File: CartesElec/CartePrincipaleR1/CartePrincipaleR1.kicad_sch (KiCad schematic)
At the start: 21 parts, among them J1 I2C, J11 Conn_01x02_Male, J12 Conn_01x04_Male, J13 Conn_01x04_Male, J2 I2C, J3 UART, J4 UART, J5 Conn_02x08_Top_Bottom, J6 Conn_02x08_Top_Bottom, J8 Conn_01x04_Male, U1 LT1129-3.3_SOT223, U2 NUCLEO64-F411RE

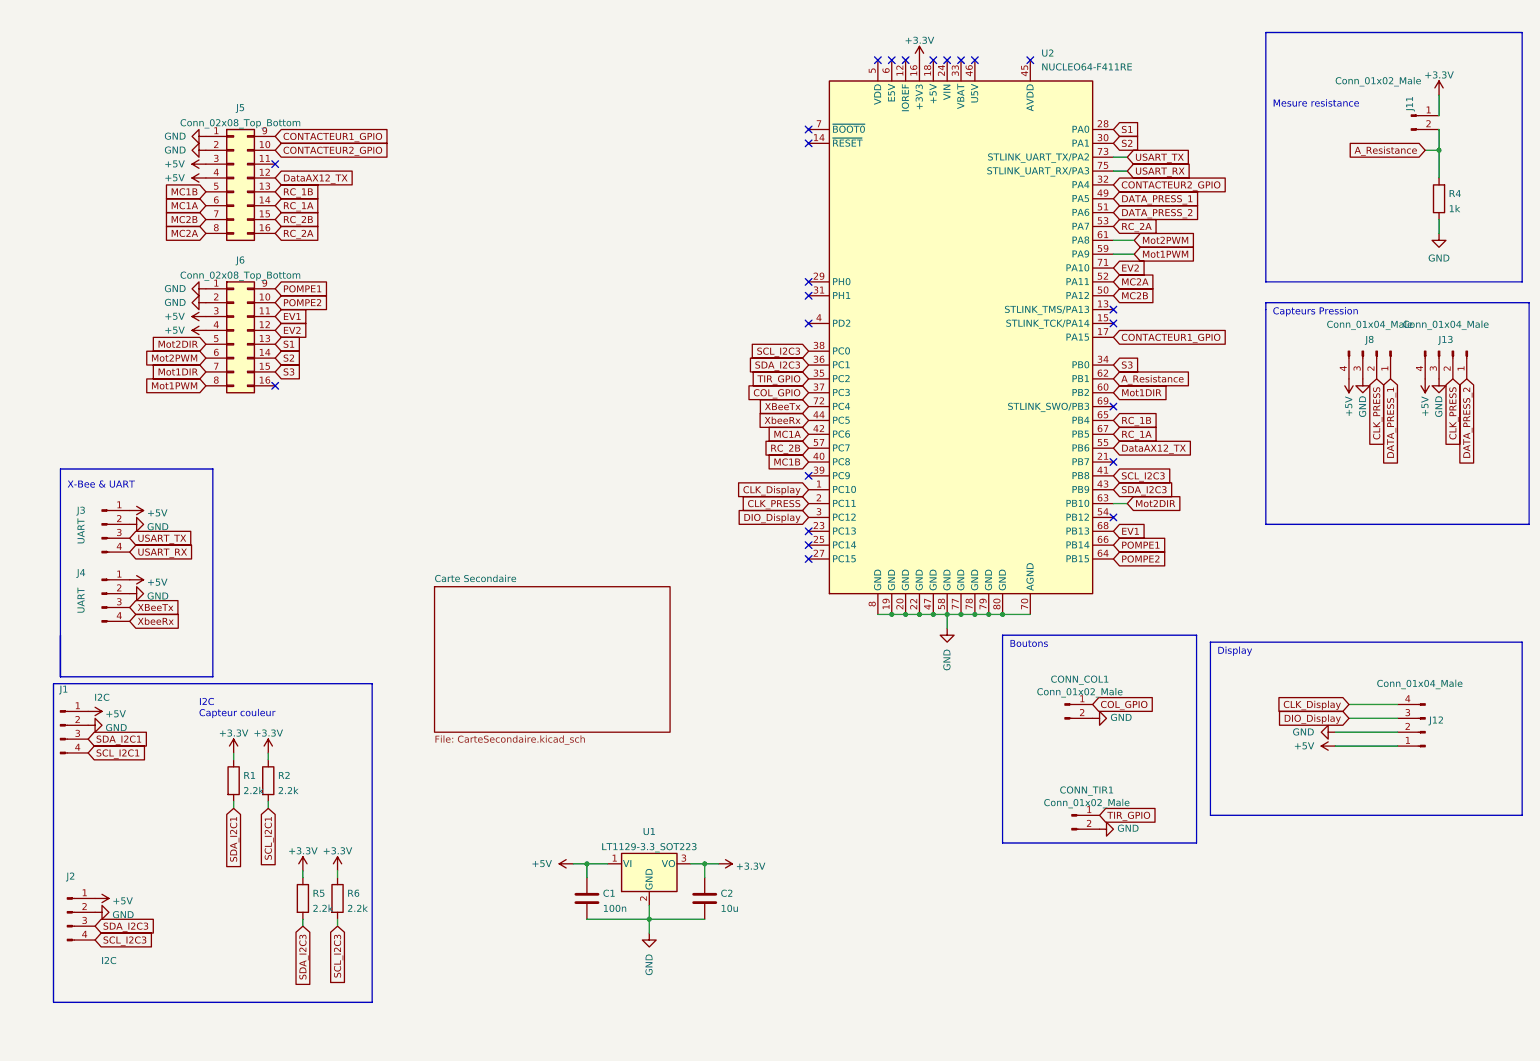
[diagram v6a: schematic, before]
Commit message: Ajout de textes au PCB
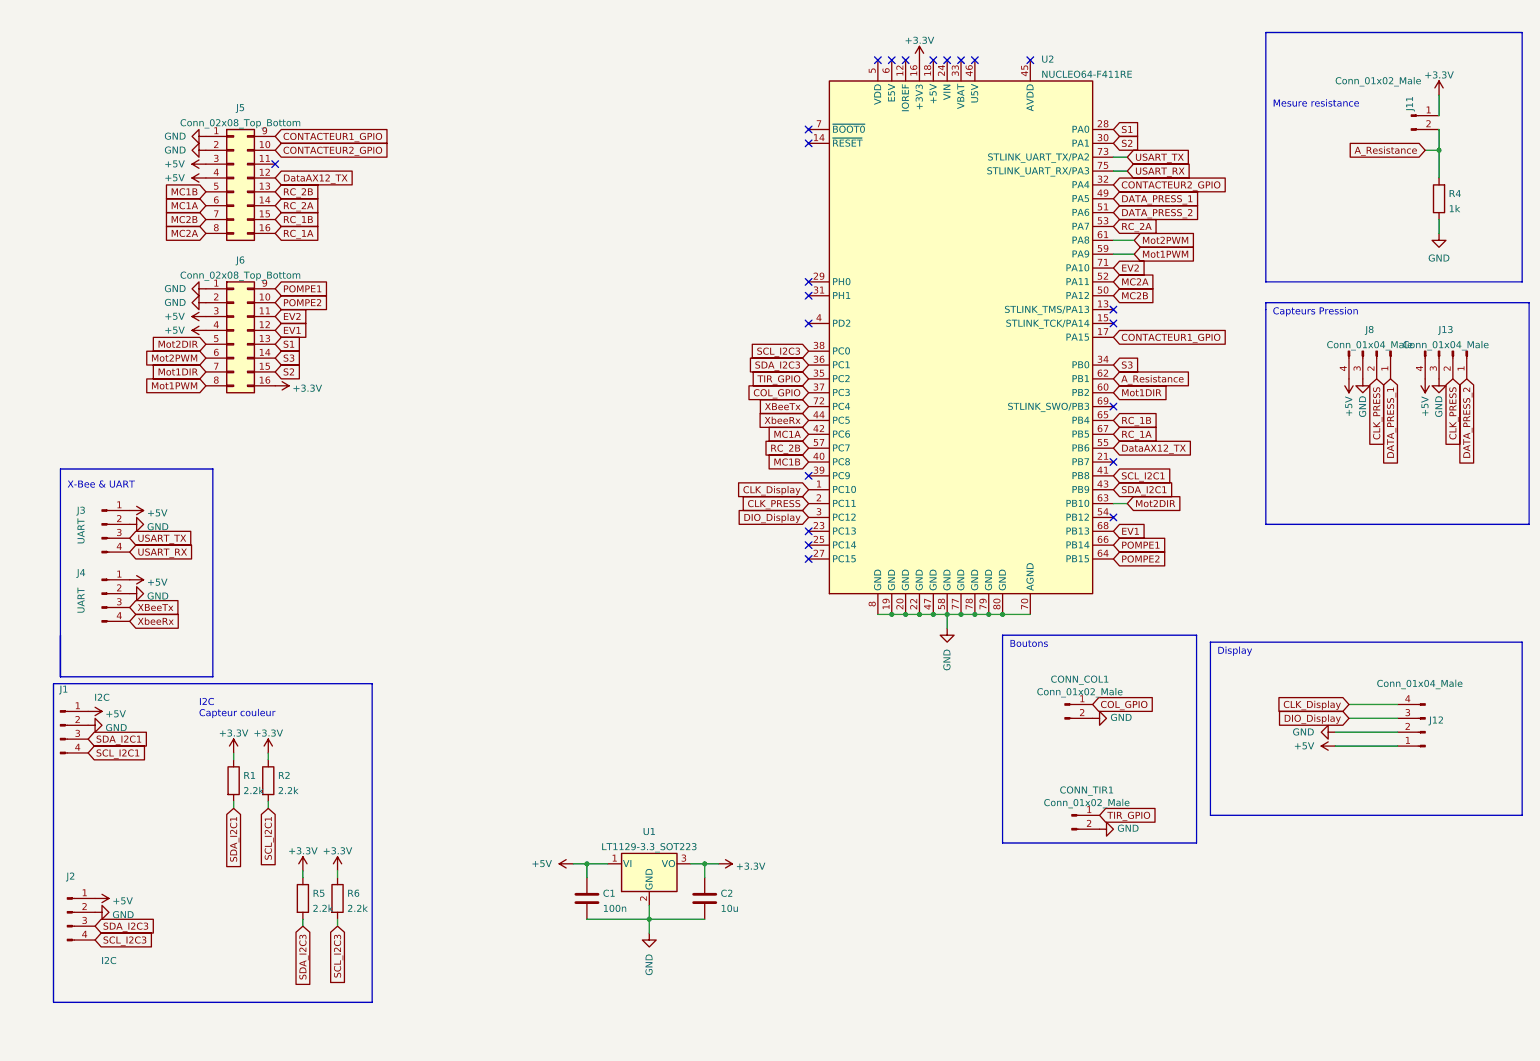
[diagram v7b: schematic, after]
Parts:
- C1, C2: footprint (none) -> Capacitor_SMD:C_0805_2012Metric
- CONN_COL1, CONN_TIR1: footprint Connector_JST:JST_XH_B2B-XH-A_1x02_P2.50mm_Vertical -> library:HE14_EMBASE_1x02
- J1, J12, J13, J2, J8: footprint (none) -> library:HE14_EMBASE_1x04
- J11: footprint (none) -> library:HE14_EMBASE_1x02
- J5, J6: footprint (none) -> Connector_IDC:IDC-Header_2x08_P2.54mm_Vertical
- R1, R2, R4, R5, R6: footprint (none) -> Resistor_SMD:R_0805_2012Metric
- U2: footprint Module:ST_Morpho_Connector_144_STLink -> library:ST_NUCLEO-F401RE
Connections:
- net +3V3: now also J6.16 (Pin_16)
- net EV1: now also J6.12 (Pin_12); no longer J6.11 (Pin_11)
- net EV2: now also J6.11 (Pin_11); no longer J6.12 (Pin_12)
- net RC_1A: now also J5.16 (Pin_16); no longer J5.14 (Pin_14)
- net RC_1B: now also J5.15 (Pin_15); no longer J5.13 (Pin_13)
- net RC_2A: now also J5.14 (Pin_14); no longer J5.16 (Pin_16)
- net RC_2B: now also J5.13 (Pin_13); no longer J5.15 (Pin_15)
- net S2: now also J6.15 (Pin_15); no longer J6.14 (Pin_14)
- net S3: now also J6.14 (Pin_14); no longer J6.15 (Pin_15)
- net SCL_I2C1: now also U2.41 (PB8)
- net SCL_I2C3: no longer U2.41 (PB8)
- net SDA_I2C1: now also U2.43 (PB9)
- net SDA_I2C3: no longer U2.43 (PB9)
- no-connect marks 24 -> 23
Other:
- removed sheet Carte Secondaire
